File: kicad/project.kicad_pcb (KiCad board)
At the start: 2 copper layers, 59 x 59 mm, 20 parts, among them J1 SWD, SW1 SW_DPDT_x2, U1 STM32L031F4Px

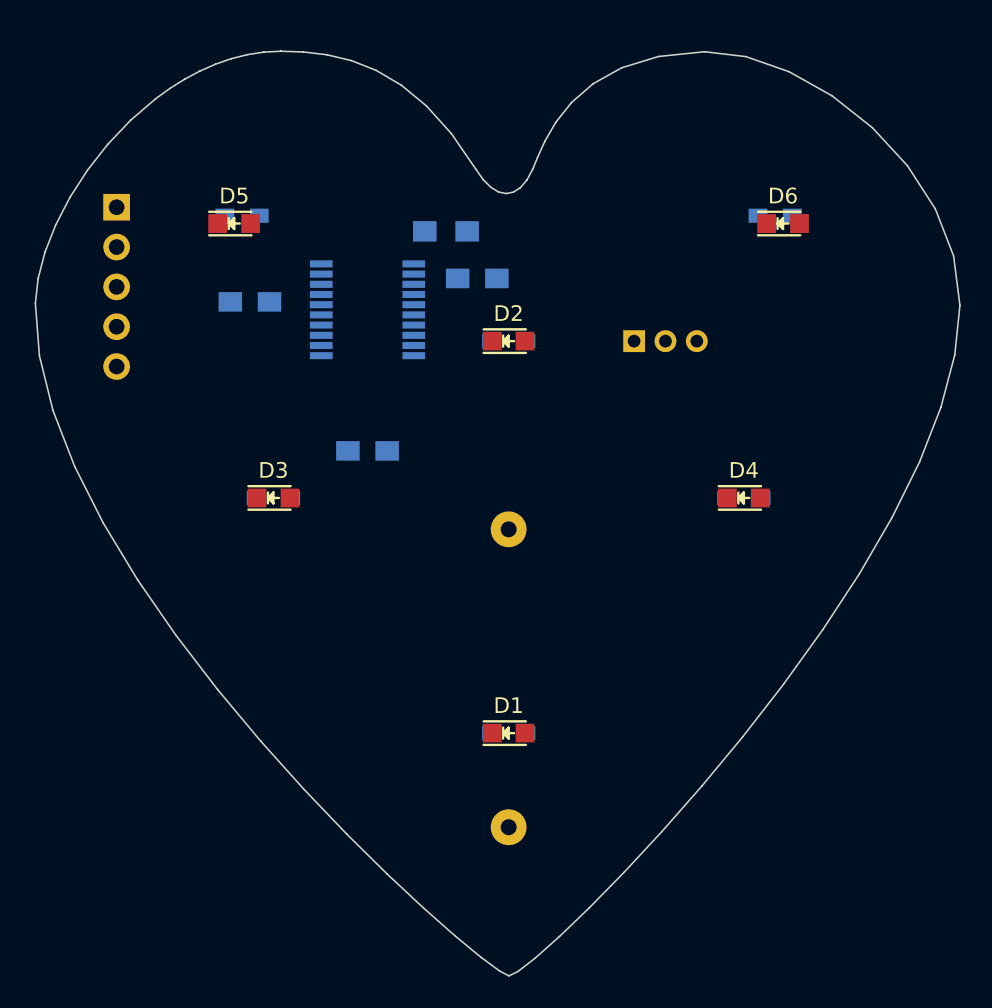
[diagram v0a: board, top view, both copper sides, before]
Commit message: Better heart outline
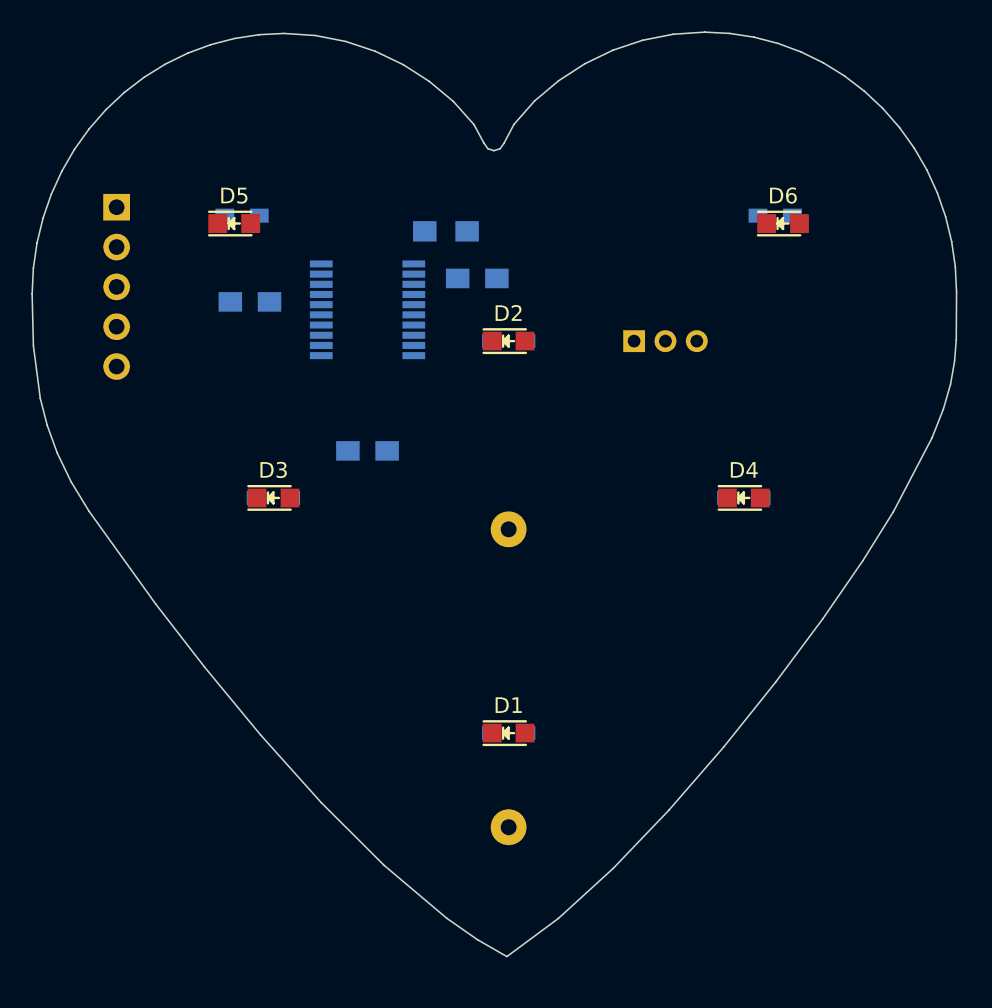
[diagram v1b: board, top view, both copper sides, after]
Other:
- outline, holes or cut-outs redrawn

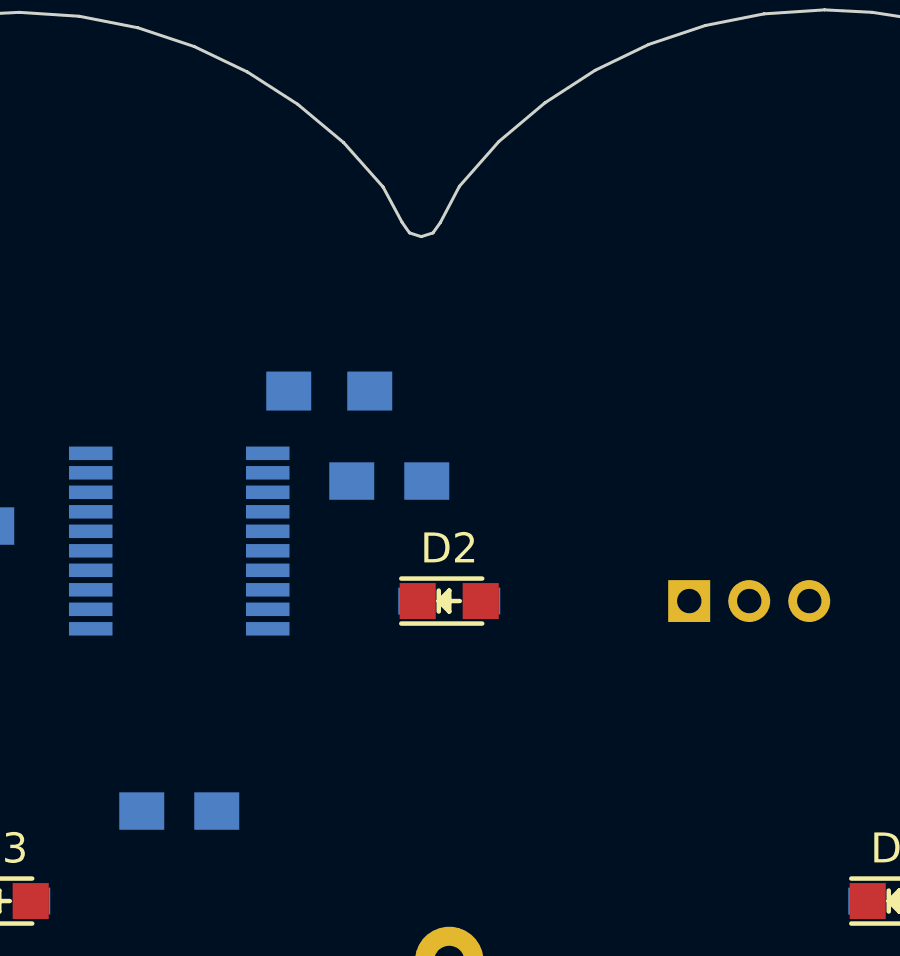
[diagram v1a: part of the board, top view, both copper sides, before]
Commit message: Optional LED footprints
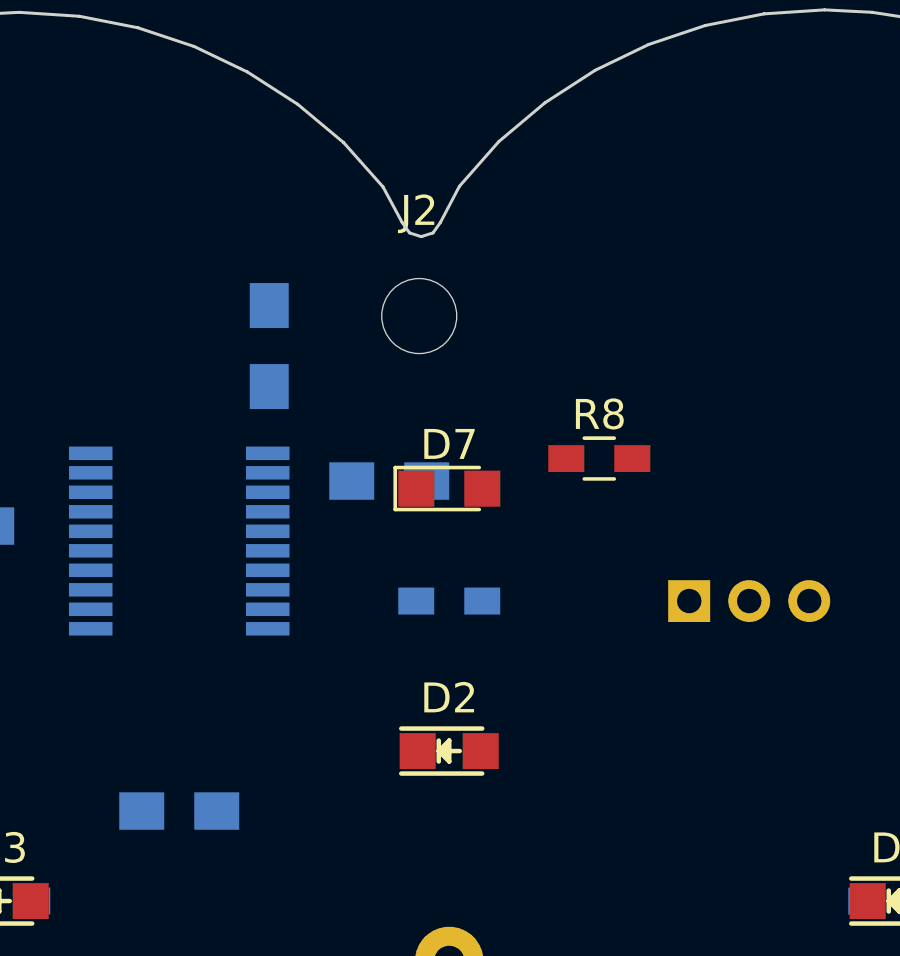
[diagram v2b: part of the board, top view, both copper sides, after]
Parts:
- added D7: LED, LEDs:LED_0805, F.Cu at (130.0, 101.2)
- added J2: Conn_01x01, Mounting_Holes:MountingHole_2.5mm, F.Cu at (129.0, 95.5)
- added R8: 1k, Resistors_SMD:R_0603_HandSoldering, F.Cu at (135.0, 100.2)
- moved D2 5.00 mm to (130.0, 110.0)
- moved R1 2.50 mm to (124.0, 96.5), turned to 90 degrees
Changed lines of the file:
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@@
 (kicad_pcb (version 4) (host pcbnew 4.0.7-e2-6376~58~ubuntu16.04.1)
   (general
-    (links 35)
-    (no_connects 35)
+    (links 39)
+    (no_connects 39)
     (area 99.561516 85.244019 158.615741 144.300151)
     (thickness 1.6)
@@
     (tracks 0)
     (zones 0)
-    (modules 20)
-    (nets 28)
+    (modules 23)
+    (nets 29)
   )
   (page A4)
@@
   (net 26 "Net-(BT1-Pad1)")
   (net 27 "Net-(SW1-Pad3)")
+  (net 28 "Net-(D7-Pad2)")
   (net_class Default "This is the default net class."
     (clearance 0.2032)
@@
     (add_net "Net-(D5-Pad2)")
     (add_net "Net-(D6-Pad2)")
+    (add_net "Net-(D7-Pad2)")
     (add_net "Net-(R1-Pad1)")
     (add_net "Net-(R2-Pad2)")
@@
   )
   (module LEDs:LED_0805 (layer F.Cu)
-    (at 130 105)
+    (at 130 110)
     (descr "LED 0805 smd package")
     (tags "LED 0805 SMD")
@@
   )
   (module Resistors_SMD:R_0805_HandSoldering (layer B.Cu)
-    (at 126 98)
+    (at 124 96.5 90)
     (descr "Resistor SMD 0805, hand soldering")
     (tags "resistor 0805")
     (attr smd)
-    (fp_text reference R1 (at 0 2.1) (layer B.SilkS)
-      (effects (font (size 1 1) (thickness 0.15)) (justify mirror))
-    )
-    (fp_text value 10K (at 0 -2.1) (layer B.Fab)
+    (fp_text reference R1 (at 0 2.1 90) (layer B.SilkS)
+      (effects (font (size 1 1) (thickness 0.15)) (justify mirror))
+    )
+    (fp_text value 10K (at 0 -2.1 90) (layer B.Fab)
       (effects (font (size 1 1) (thickness 0.15)) (justify mirror))
     )
@@
     (fp_line (start 0.6 -0.875) (end -0.6 -0.875) (layer B.SilkS) (width 0.15))
     (fp_line (start -0.6 0.875) (end 0.6 0.875) (layer B.SilkS) (width 0.15))
-    (pad 1 smd rect (at -1.35 0) (size 1.5 1.3) (layers B.Cu B.Paste B.Mask)
+    (pad 1 smd rect (at -1.35 0 90) (size 1.5 1.3) (layers B.Cu B.Paste B.Mask)
       (net 12 "Net-(R1-Pad1)"))
-    (pad 2 smd rect (at 1.35 0) (size 1.5 1.3) (layers B.Cu B.Paste B.Mask)
+    (pad 2 smd rect (at 1.35 0 90) (size 1.5 1.3) (layers B.Cu B.Paste B.Mask)
       (net 2 GND))
     (model Resistors_SMD.3dshapes/R_0805_HandSoldering.wrl
@@
       (net 26 "Net-(BT1-Pad1)"))
   )
+  (module LEDs:LED_0805 (layer F.Cu)
+    (at 130 101.25)
+    (descr "LED 0805 smd package")
+    (tags "LED led 0805 SMD smd SMT smt smdled SMDLED smtled SMTLED")
+    (attr smd)
+    (fp_text reference D7 (at 0 -1.45) (layer F.SilkS)
+      (effects (font (size 1 1) (thickness 0.15)))
+    )
+    (fp_text value LED (at 0 1.55) (layer F.Fab)
+      (effects (font (size 1 1) (thickness 0.15)))
+    )
+    (fp_line (start -1.8 -0.7) (end -1.8 0.7) (layer F.SilkS) (width 0.12))
+    (fp_line (start -0.4 -0.4) (end -0.4 0.4) (layer F.Fab) (width 0.1))
+    (fp_line (start -0.4 0) (end 0.2 -0.4) (layer F.Fab) (width 0.1))
+    (fp_line (start 0.2 0.4) (end -0.4 0) (layer F.Fab) (width 0.1))
+    (fp_line (start 0.2 -0.4) (end 0.2 0.4) (layer F.Fab) (width 0.1))
+    (fp_line (start 1 0.6) (end -1 0.6) (layer F.Fab) (width 0.1))
+    (fp_line (start 1 -0.6) (end 1 0.6) (layer F.Fab) (width 0.1))
+    (fp_line (start -1 -0.6) (end 1 -0.6) (layer F.Fab) (width 0.1))
+    (fp_line (start -1 0.6) (end -1 -0.6) (layer F.Fab) (width 0.1))
+    (fp_line (start -1.8 0.7) (end 1 0.7) (layer F.SilkS) (width 0.12))
+    (fp_line (start -1.8 -0.7) (end 1 -0.7) (layer F.SilkS) (width 0.12))
+    (fp_line (start 1.95 -0.85) (end 1.95 0.85) (layer F.CrtYd) (width 0.05))
+    (fp_line (start 1.95 0.85) (end -1.95 0.85) (layer F.CrtYd) (width 0.05))
+    (fp_line (start -1.95 0.85) (end -1.95 -0.85) (layer F.CrtYd) (width 0.05))
+    (fp_line (start -1.95 -0.85) (end 1.95 -0.85) (layer F.CrtYd) (width 0.05))
+    (fp_text user %R (at 0 -1.25) (layer F.Fab)
+      (effects (font (size 0.4 0.4) (thickness 0.1)))
+    )
+    (pad 2 smd rect (at 1.1 0 180) (size 1.2 1.2) (layers F.Cu F.Paste F.Mask)
+      (net 28 "Net-(D7-Pad2)"))
+    (pad 1 smd rect (at -1.1 0 180) (size 1.2 1.2) (layers F.Cu F.Paste F.Mask)
+      (net 2 GND))
+    (model ${KISYS3DMOD}/LEDs.3dshapes/LED_0805.wrl
+      (at (xyz 0 0 0))
+      (scale (xyz 1 1 1))
+      (rotate (xyz 0 0 180))
+    )
+  )
+  (module Resistors_SMD:R_0603_HandSoldering (layer F.Cu)
+    (at 135 100.25)
+    (descr "Resistor SMD 0603, hand soldering")
+    (tags "resistor 0603")
+    (attr smd)
+    (fp_text reference R8 (at 0 -1.45) (layer F.SilkS)
+      (effects (font (size 1 1) (thickness 0.15)))
+    )
+    (fp_text value 1k (at 0 1.55) (layer F.Fab)
+      (effects (font (size 1 1) (thickness 0.15)))
+    )
+    (fp_text user %R (at 0 0) (layer F.Fab)
+      (effects (font (size 0.4 0.4) (thickness 0.075)))
+    )
+    (fp_line (start -0.8 0.4) (end -0.8 -0.4) (layer F.Fab) (width 0.1))
+    (fp_line (start 0.8 0.4) (end -0.8 0.4) (layer F.Fab) (width 0.1))
+    (fp_line (start 0.8 -0.4) (end 0.8 0.4) (layer F.Fab) (width 0.1))
+    (fp_line (start -0.8 -0.4) (end 0.8 -0.4) (layer F.Fab) (width 0.1))
+    (fp_line (start 0.5 0.68) (end -0.5 0.68) (layer F.SilkS) (width 0.12))
+    (fp_line (start -0.5 -0.68) (end 0.5 -0.68) (layer F.SilkS) (width 0.12))
+    (fp_line (start -1.96 -0.7) (end 1.95 -0.7) (layer F.CrtYd) (width 0.05))
+    (fp_line (start -1.96 -0.7) (end -1.96 0.7) (layer F.CrtYd) (width 0.05))
+    (fp_line (start 1.95 0.7) (end 1.95 -0.7) (layer F.CrtYd) (width 0.05))
+    (fp_line (start 1.95 0.7) (end -1.96 0.7) (layer F.CrtYd) (width 0.05))
+    (pad 1 smd rect (at -1.1 0) (size 1.2 0.9) (layers F.Cu F.Paste F.Mask)
+      (net 28 "Net-(D7-Pad2)"))
+    (pad 2 smd rect (at 1.1 0) (size 1.2 0.9) (layers F.Cu F.Paste F.Mask)
+      (net 19 "Net-(R8-Pad2)"))
+    (model ${KISYS3DMOD}/Resistors_SMD.3dshapes/R_0603.wrl
+      (at (xyz 0 0 0))
+      (scale (xyz 1 1 1))
+      (rotate (xyz 0 0 0))
+    )
+  )
+  (module Mounting_Holes:MountingHole_2.5mm (layer F.Cu)
+    (at 129 95.5)
+    (descr "Mounting Hole 2.5mm, no annular")
+    (tags "mounting hole 2.5mm no annular")
+    (attr virtual)
+    (fp_text reference J2 (at 0 -3.5) (layer F.SilkS)
+      (effects (font (size 1 1) (thickness 0.15)))
+    )
+    (fp_text value Conn_01x01 (at 0 3.5) (layer F.Fab)
+      (effects (font (size 1 1) (thickness 0.15)))
+    )
+    (fp_text user %R (at 0.3 0) (layer F.Fab)
+      (effects (font (size 1 1) (thickness 0.15)))
+    )
+    (fp_circle (center 0 0) (end 2.5 0) (layer Cmts.User) (width 0.15))
+    (fp_circle (center 0 0) (end 2.75 0) (layer F.CrtYd) (width 0.05))
+    (pad 1 np_thru_hole circle (at 0 0) (size 2.5 2.5) (drill 2.5) (layers *.Cu *.Mask)
+      (net 2 GND))
+  )
   (gr_line (start 142.50999 85.29402) (end 142.50999 85.29402) (layer Edge.Cuts) (width 0.1))

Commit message: LEDs layout
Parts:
- removed D7: LED, LEDs:LED_0805
- removed R8: 1k, Resistors_SMD:R_0603_HandSoldering
- added D10: LED, LEDs:LED_D5.0mm, F.Cu at (113.0, 115.0)
- added D11: LED, LEDs:LED_D5.0mm, F.Cu at (145.0, 115.0)
- added D12: LED, LEDs:LED_D5.0mm, F.Cu at (112.0, 96.0)
- added D13: LED, LEDs:LED_D5.0mm, F.Cu at (146.0, 96.0)
- added D15: LED, LEDs:LED_1206, F.Cu at (130.0, 127.0)
- added D16: LED, LEDs:LED_1206, F.Cu at (130.0, 107.0)
- added D17: LED, LEDs:LED_1206, F.Cu at (114.0, 113.0)
- added D18: LED, LEDs:LED_1206, F.Cu at (146.0, 113.0)
- added D19: LED, LEDs:LED_1206, F.Cu at (113.0, 94.0)
- added D20: LED, LEDs:LED_1206, F.Cu at (147.0, 94.0)
- added D8: LED, LEDs:LED_D5.0mm, F.Cu at (129.0, 129.0)
- added D9: LED, LEDs:LED_D5.0mm, F.Cu at (129.0, 109.0)
- J1: value SWD -> Conn_01x05; footprint Pin_Headers:Pin_Header_Straight_1x05_Pitch2.54mm -> Pin_Header_Straight_1x05_Pitch2.54mm
- SW1: footprint SW_Micro_SPST -> Buttons_Switches_THT:SW_Micro_SPST
- moved R2 21.5 mm to (120.0, 111.0), turned to 90 degrees
- moved C1 7.07 mm to (114.0, 111.0)
- moved R6 5.00 mm to (113.0, 92.0)
- moved R7 5.00 mm to (147.0, 92.0)
- moved R5 4.12 mm to (146.0, 111.0)
- moved D3 2.24 mm to (114.0, 117.0)
- moved D4 2.24 mm to (146.0, 117.0)
- moved J2 1.12 mm to (130.0, 96.0)
- moved D1 1.00 mm to (130.0, 131.0)
- moved D2 1.00 mm to (130.0, 111.0)
- moved D5 0.71 mm to (113.0, 98.0)
- moved D6 0.71 mm to (147.0, 98.0)
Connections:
- J1 pad 1: NRST -> +BATT
- J1 pad 2: SWDIO -> SWCLK
- J1 pad 4: SWCLK -> SWDIO
- J1 pad 5: +BATT -> NRST

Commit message: Routing
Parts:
- J1: footprint Pin_Header_Straight_1x05_Pitch2.54mm -> Pin_Headers:Pin_Header_Straight_1x05_Pitch2.54mm
- moved C1 28.7 mm to (141.3, 102.0), turned to 0 degrees
- moved R2 20.0 mm to (140.0, 110.9)
- moved R6 9.58 mm to (121.4, 96.6), turned to 270 degrees
- moved R4 5.26 mm to (118.3, 110.9), turned to 90 degrees
- moved C3 1.94 mm to (126.4, 99.9), turned to 270 degrees
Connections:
- net Net-(BT1-Pad1) renamed /BATT_UNSWITCHED
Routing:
- net GND: track 0.00 -> 191.3 mm, vias 0 -> 4
- net +BATT: track 0.00 -> 74.3 mm, vias 0 -> 1
- net Net-(R7-Pad2): track 0.00 -> 39.2 mm
- net /BATT_UNSWITCHED: track 0.00 -> 38.2 mm
- net Net-(R5-Pad2): track 0.00 -> 35.5 mm
- net Net-(D1-Pad2): track 0.00 -> 24.9 mm
- net NRST: track 0.00 -> 20.9 mm, vias 0 -> 1
- net Net-(R2-Pad2): track 0.00 -> 18.5 mm
- net SWDIO: track 0.00 -> 14.4 mm
- net SWCLK: track 0.00 -> 13.5 mm
- net Net-(D12-Pad2): track 0.00 -> 11.5 mm
- net Net-(R6-Pad2): track 0.00 -> 9.54 mm
- net Net-(D16-Pad2): track 0.00 -> 8.92 mm, vias 0 -> 1
- net Net-(D13-Pad2): track 0.00 -> 8.43 mm
- net Net-(D11-Pad2): track 0.00 -> 8.43 mm
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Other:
- net class Wide: clearance 0.254 -> 0.22; trace_width 0.3556 -> 0.35

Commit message: Switches
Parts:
- added R8: 1k, Resistors_SMD:R_0603_HandSoldering, B.Cu at (108.5, 115.1)
- added SW2: SW_SPDT, Buttons_Switches_THT:SW_Micro_SPST, B.Cu at (140.0, 102.0)
- added SW3: SW_Push, Buttons_Switches_THT:SW_PUSH_6mm, B.Cu at (108.2, 109.8)
- J1: footprint Pin_Headers:Pin_Header_Straight_1x05_Pitch2.54mm -> SWD_Header
- J2: footprint Mounting_Holes:MountingHole_2.5mm -> Mounting_Holes:MountingHole_2.5mm_Pad
- SW1: value SW_DPDT_x2 -> SW_SPDT; footprint Buttons_Switches_THT:SW_Micro_SPST -> theapi:SW_Micro_SPST
- moved C1 5.50 mm to (141.2, 107.5)
- moved C3 1.36 mm to (126.2, 101.2)
- moved C2 0.56 mm to (113.0, 102.2)
- moved D13 0.35 mm to (146.2, 95.8)
- moved R6 0.14 mm to (121.5, 96.5)
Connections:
- net +BATT renamed BATT_SW
- net /BATT_UNSWITCHED renamed /BATT+
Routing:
- net GND: track 191.3 -> 215.2 mm, vias 4 -> 5
- net Net-(SW3-Pad1): track 0.00 -> 17.6 mm, vias 0 -> 1
- net Net-(R8-Pad2): track 0.00 -> 16.8 mm
- net BATT_SW: track 74.3 -> 66.4 mm
- net /BATT+: track 38.2 -> 40.7 mm
- net NRST: track 20.9 -> 22.4 mm, vias 1 -> 2
- net Net-(R5-Pad2): track 35.5 -> 34.8 mm
- net Net-(R6-Pad2): track 9.54 -> 10.1 mm
